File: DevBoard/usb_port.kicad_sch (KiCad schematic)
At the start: 105 parts, among them J501 TYPE-C 16PCB0.8 IP68, J502 I2CC logic analyzer, Q501 IAUC45N04S6L063H, Q502 IAUC45N04S6L063H, U501 TPS25751DREFR, U502 M24512-DFMC6TG, U503 BQ25756RRVR, U504 TPS62933DRLR

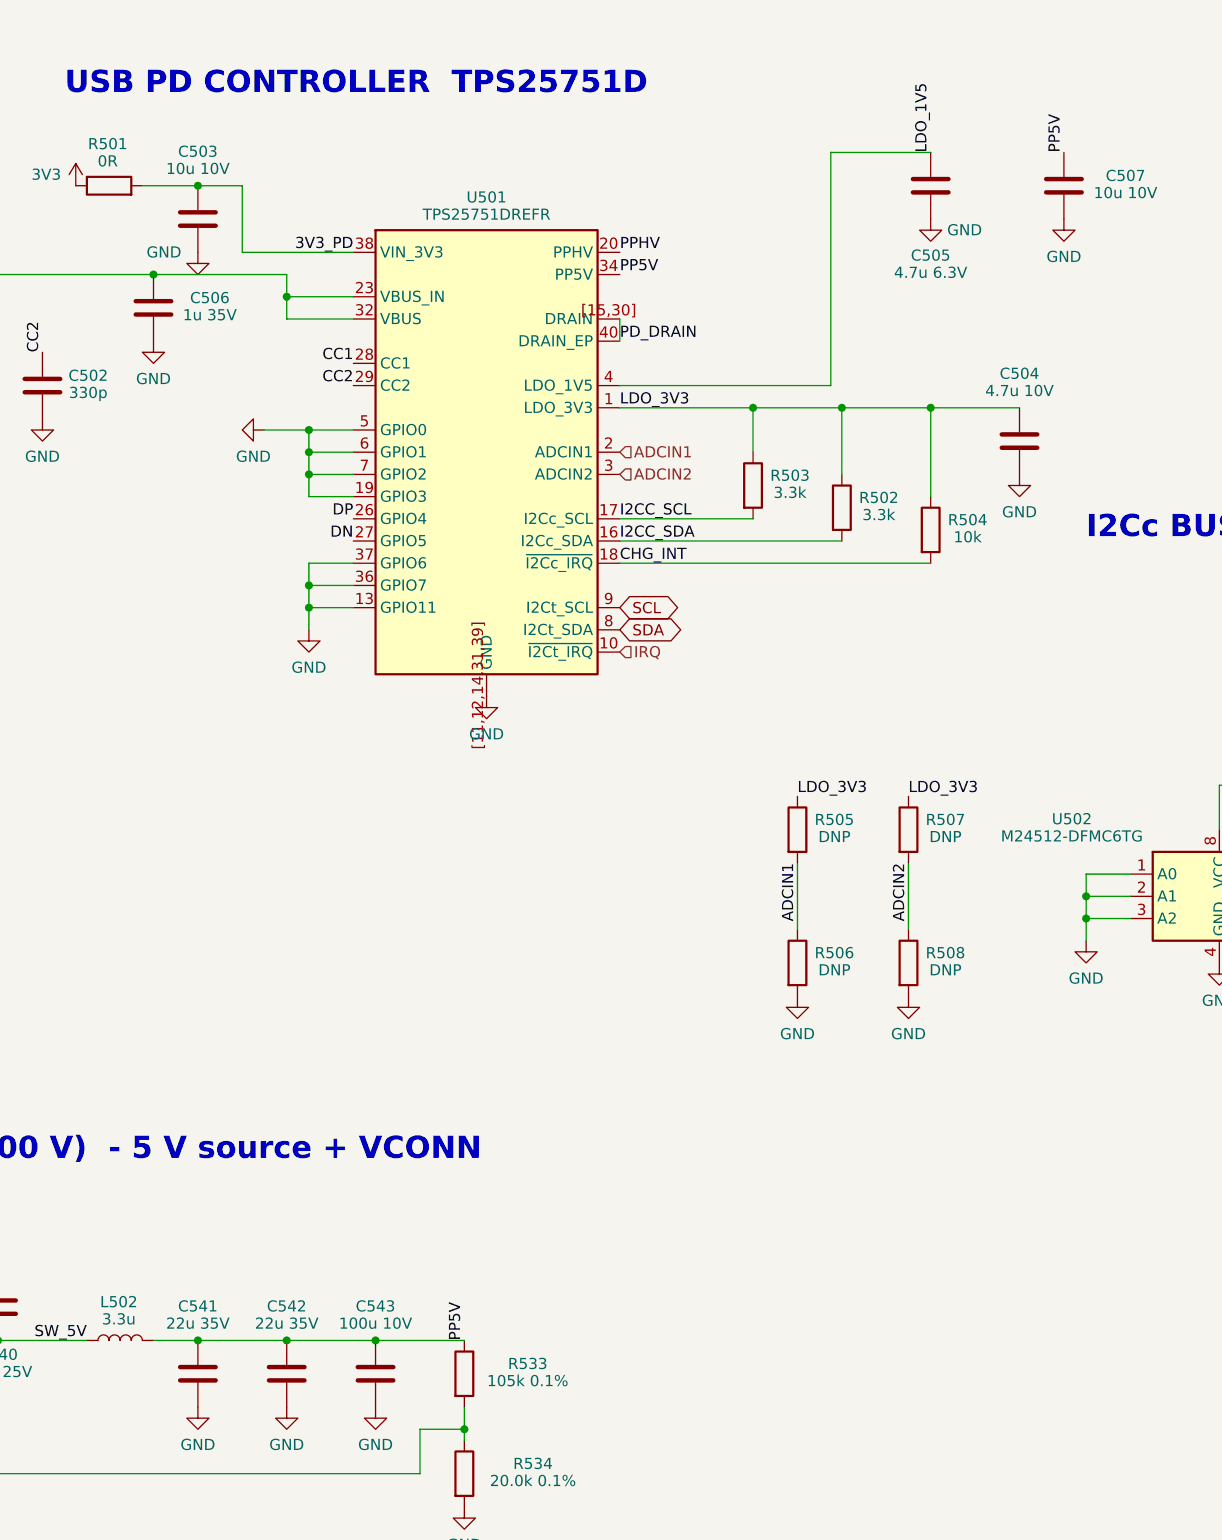
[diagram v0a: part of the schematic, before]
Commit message: Dev board: choose fuse, gauge diode and TPS25751 capacitor values
- F101: 1206FA-8A (C21261118), 1206, 32 V, 300 A interrupt; D101: BAT54WS (C7502694)
- TPS25751 caps per datasheet table 6.4 (after derating): LDO_3V3 and LDO_1V5
  to 10 uF, VBUS to 4.7 uF 50 V 0805, PP5V bulk to a 220 uF polymer
- README: PPHV bulk vs cSnkBulkPd and INA190 stock as open items

Co-Authored-By: Claude Opus 5.5 <noreply@anthropic.com>
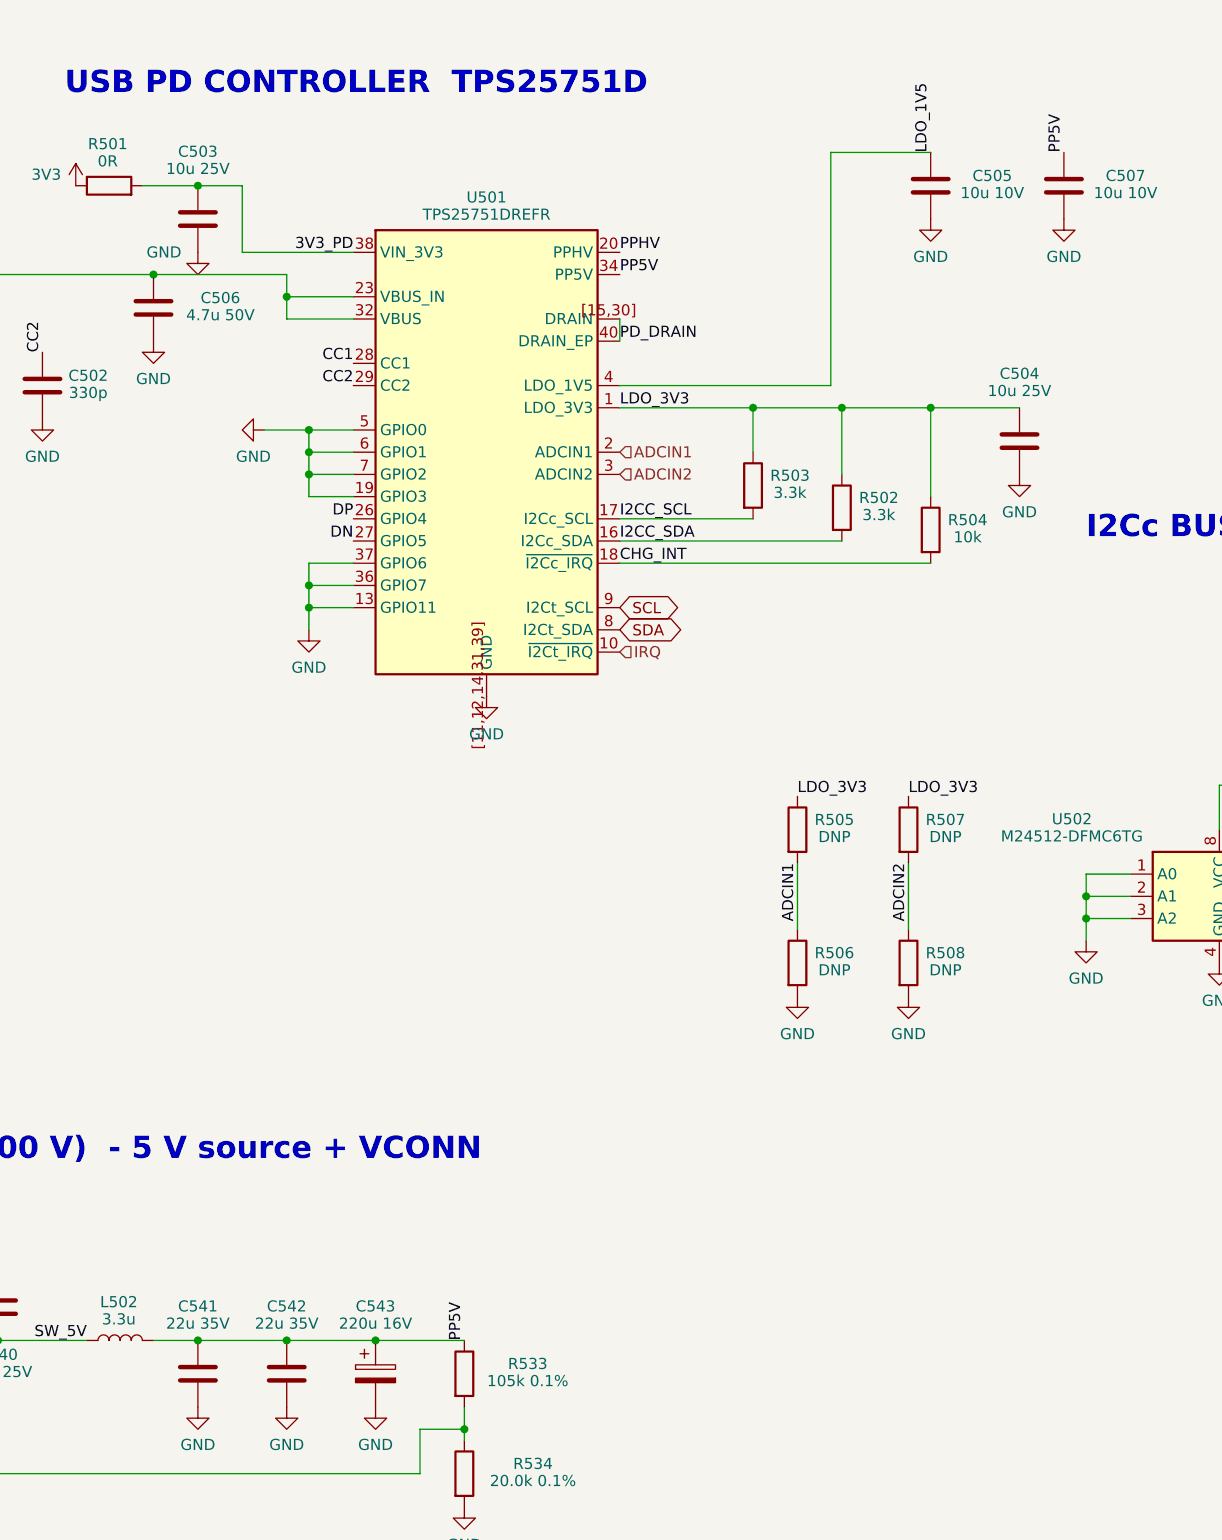
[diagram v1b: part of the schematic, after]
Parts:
- C503: value 10u 10V -> 10u 25V; LCSC (none) -> C15850
- C504: value 4.7u 10V -> 10u 25V; footprint Capacitor_SMD:C_0603_1608Metric -> Capacitor_SMD:C_0805_2012Metric; LCSC (none) -> C15850; Notes (none) -> LDO_3V3: TPS25751 needs 5 uF min after derating
- C505: value 4.7u 6.3V -> 10u 10V; LCSC (none) -> C19702; Notes (none) -> LDO_1V5: 4.5-12 uF effective
- C506: value 1u 35V -> 4.7u 50V; footprint Capacitor_SMD:C_0603_1608Metric -> Capacitor_SMD:C_0805_2012Metric; LCSC (none) -> C20416422; Notes (none) -> VBUS: 1-10 uF effective, 25 V+ rating
- C543: value 100u 10V -> 220u 16V; footprint Capacitor_SMD:C_1210_3225Metric -> Capacitor_SMD:CP_Elec_6.3x7.7; symbol Device:C -> Device:C_Polarized; LCSC (none) -> C25503905; MPN (none) -> ChuangHui SS221M160E7R7R4Z00ZZ (polymer); Notes PP5V bulk -> PP5V bulk: USB PD cSrcBulkShared needs 120 uF; polymer has 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
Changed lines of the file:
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@@
 	)
 	(junction
+		(at 438.15 220.98)
+		(diameter 0)
+		(color 0 0 0 0)
+	)
+	(junction
 		(at 410.21 76.2)
 		(diameter 0)
@@
 	)
 	(symbol
-		(lib_id "Device:C")
+		(lib_id "Device:C_Polarized")
 		(at 157.48 207.01 0)
 		(unit 1)
@@
 			)
 		)
-		(property "Value" "100u 10V"
+		(property "Value" "220u 16V"
 			(at 157.48 201.27 0)
 			(show_name no)
@@
 			)
 		)
-		(property "Footprint" "Capacitor_SMD:C_1210_3225Metric"
+		(property "Footprint" "Capacitor_SMD:CP_Elec_6.3x7.7"
 			(at 158.445 203.2 0)
 			(hide yes)
@@
 			)
 		)
-		(property "Notes" "PP5V bulk"
+		(property "Notes" "PP5V bulk: USB PD cSrcBulkShared needs 120 uF; polymer has no DC-bias loss"
 			(at 0 0 0)
 			(hide yes)
@@
 			)
 		)
+		(property "LCSC" "C25503905"
+			(at 157.48 207.01 0)
+			(hide yes)
+			(show_name no)
+			(do_not_autoplace no)
+			(effects
+				(font
+					(size 1.27 1.27)
+				)
+			)
+		)
+		(property "MPN" "ChuangHui SS221M160E7R7R4Z00ZZ (polymer)"
+			(at 157.48 207.01 0)
+			(hide yes)
+			(show_name no)
+			(do_not_autoplace no)
+			(effects
+				(font
+					(size 1.27 1.27)
+				)
+			)
+		)
 		(pin "1"
 		)
@@
 		(dnp no)
 		(property "Reference" "C506"
-			(at 138.53 83.96 0)
+			(at 139.74 83.96 0)
 			(show_name no)
 			(do_not_autoplace no)
@@
 			)
 		)
-		(property "Value" "1u 35V"
-			(at 138.53 85.92 0)
+		(property "Value" "4.7u 50V"
+			(at 139.74 85.92 0)
 			(show_name no)
 			(do_not_autoplace no)
@@
 			)
 		)
-		(property "Footprint" "Capacitor_SMD:C_0603_1608Metric"
+		(property "Footprint" "Capacitor_SMD:C_0805_2012Metric"
 			(at 133.045 81.28 0)
 			(hide yes)
@@
 			)
 		)
+		(property "LCSC" "C20416422"
+			(at 132.08 85.09 0)
+			(hide yes)
+			(show_name no)
+			(do_not_autoplace no)
+			(effects
+				(font
+					(size 1.27 1.27)
+				)
+			)
+		)
+		(property "Notes" "VBUS: 1-10 uF effective, 25 V+ rating"
+			(at 132.08 85.09 0)
+			(hide yes)
+			(show_name no)
+			(do_not_autoplace no)
+			(effects
+				(font
+					(size 1.27 1.27)
+				)
+			)
+		)
 		(pin "1"
 		)
@@
 		)
 		(property "Value" "GND"
-			(at 224.86 76.20 0)
+			(at 220.98 79.25 0)
 			(show_name no)
 			(do_not_autoplace no)
@@
 			)
 		)
-		(property "Value" "10u 10V"
+		(property "Value" "10u 25V"
 			(at 137.16 69.19 0)
 			(show_name no)
@@
 			)
 		)
+		(property "LCSC" "C15850"
+			(at 137.16 74.93 0)
+			(hide yes)
+			(show_name no)
+			(do_not_autoplace no)
+			(effects
+				(font
+					(size 1.27 1.27)
+				)
+			)
+		)
 		(pin "1"
 		)
@@
 			)
 		)
-		(property "Value" "4.7u 10V"
+		(property "Value" "10u 25V"
 			(at 231.14 94.59 0)
 			(show_name no)
@@
 			)
 		)
-		(property "Footprint" "Capacitor_SMD:C_0603_1608Metric"
+		(property "Footprint" "Capacitor_SMD:C_0805_2012Metric"
 			(at 232.105 96.52 0)
 			(hide yes)
@@
 			)
 		)
+		(property "LCSC" "C15850"
+			(at 231.14 100.33 0)
+			(hide yes)
+			(show_name no)
+			(do_not_autoplace no)
+			(effects
+				(font
+					(size 1.27 1.27)
+				)
+			)
+		)
+		(property "Notes" "LDO_3V3: TPS25751 needs 5 uF min after derating"
+			(at 231.14 100.33 0)
+			(hide yes)
+			(show_name no)
+			(do_not_autoplace no)
+			(effects
+				(font
+					(size 1.27 1.27)
+				)
+			)
+		)
 		(pin "1"
 		)
@@
 		(dnp no)
 		(property "Reference" "C505"
-			(at 220.98 79.10 0)
+			(at 228.03 69.99 0)
 			(show_name no)
 			(do_not_autoplace no)
@@
 			)
 		)
-		(property "Value" "4.7u 6.3V"
-			(at 220.98 81.07 0)
+		(property "Value" "10u 10V"
+			(at 228.03 71.95 0)
 			(show_name no)
 			(do_not_autoplace no)
@@
 			)
 		)
+		(property "LCSC" "C19702"
+			(at 220.98 71.12 0)
+			(hide yes)
+			(show_name no)
+			(do_not_autoplace no)
+			(effects
+				(font
+					(size 1.27 1.27)
+				)
+			)
+		)
+		(property "Notes" "LDO_1V5: 4.5-12 uF effective"
+			(at 220.98 71.12 0)
+			(hide yes)
+			(show_name no)
+			(do_not_autoplace no)
+			(effects
+				(font
+					(size 1.27 1.27)
+				)
+			)
+		)
 		(pin "1"
 		)
@@
 		)
 	)
-	(junction
-		(at 438.15 220.98)
-		(diameter 0)
-		(color 0 0 0 0)
-	)
 	(sheet_instances
